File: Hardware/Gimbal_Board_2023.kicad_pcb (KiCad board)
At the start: 2 copper layers, 139 x 93.5 mm, 72 parts, among them J1 6P6C, J2 RJ45_LED_Shielded, Q1 Q_NMOS_GDS, Q2 Q_NMOS_GDS, Q3 Q_NMOS_GDS, Q4 Q_NMOS_GDS, Q5 Q_NMOS_GDS, Q6 Q_NMOS_GDS, Q7 Q_NMOS_GDS, SW1 SW_Push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

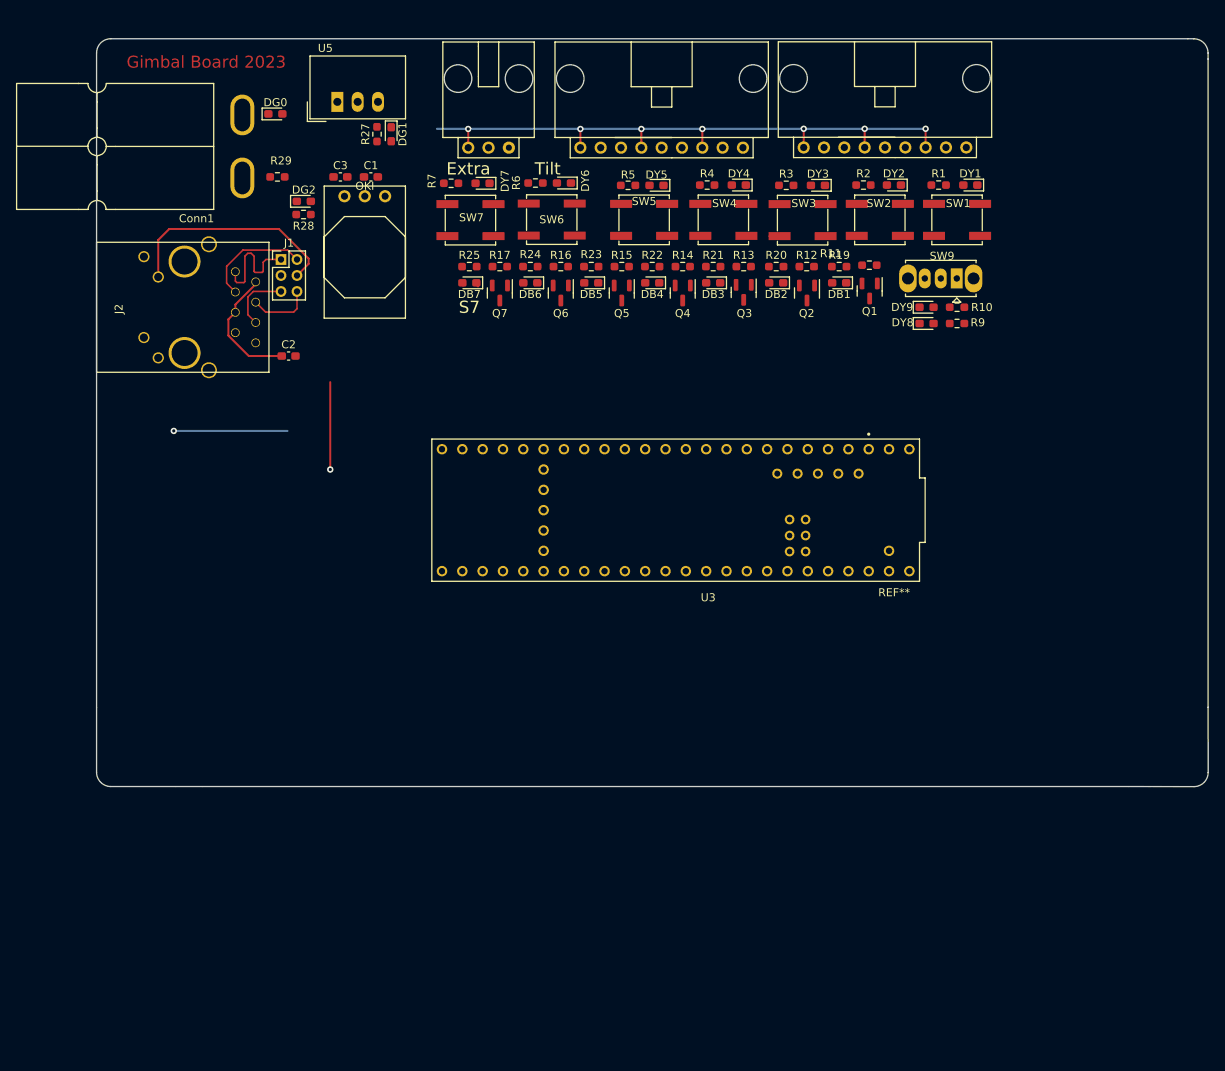
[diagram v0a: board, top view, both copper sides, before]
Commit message: Named some switches and added in volt line
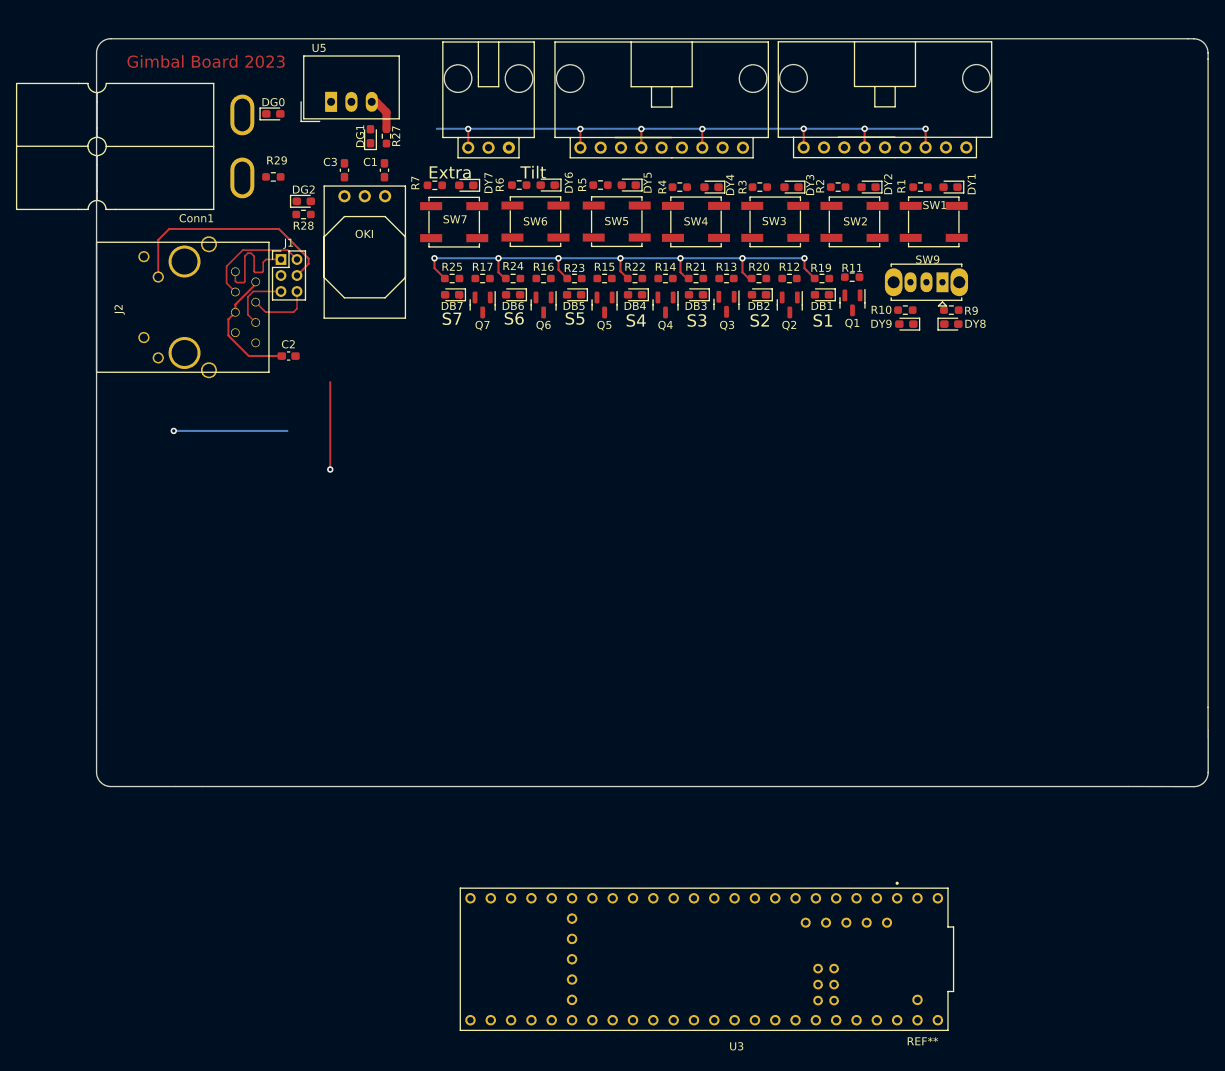
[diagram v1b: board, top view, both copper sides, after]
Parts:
- moved U3 56.2 mm to (191.0, 186.4)
- moved R10 6.47 mm to (165.4, 69.7)
- moved DY5 3.47 mm to (130.8, 54.1)
- moved R5 3.45 mm to (127.3, 54.1)
- moved DY4 3.43 mm to (141.1, 54.4)
- moved R4 3.43 mm to (137.2, 54.4)
- moved SW4 3.43 mm to (139.2, 58.7)
- moved SW3 3.43 mm to (149.1, 58.7)
- moved SW5 3.43 mm to (129.3, 58.7)
- moved DY3 3.31 mm to (151.1, 54.4)
- moved R3 3.31 mm to (147.2, 54.4)
- moved DY9 3.29 mm to (165.5, 71.5), turned to 180 degrees
- moved DY2 3.18 mm to (160.8, 54.4)
- moved R2 3.18 mm to (157.0, 54.4)
- moved SW2 3.18 mm to (159.0, 58.7)
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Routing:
- net +5V: track 77.6 -> 149.5 mm, vias 7 -> 14
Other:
- board text added: "S1"
- board text added: "S2"
- board text added: "S3"
- board text added: "S4"
- board text added: "S5"
- board text added: "S6"

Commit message: wiring
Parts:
- moved U3 67.6 mm to (187.7, 118.9)
- moved DY8 49.7 mm to (121.4, 71.3)
- moved DY9 49.7 mm to (115.8, 71.3)
- moved R10 49.7 mm to (115.7, 69.6)
- moved R9 49.7 mm to (121.4, 69.6)
- moved SW9 49.7 mm to (120.3, 66.1)
- moved Q3 30.5 mm to (173.5, 67.7)
- moved R13 30.5 mm to (173.5, 64.5)
- moved DB3 29.9 mm to (169.1, 66.5)
- moved R21 29.9 mm to (169.1, 64.5)
- moved Q6 28.0 mm to (148.1, 67.9)
- moved R16 28.0 mm to (148.1, 64.6)
- moved DB6 27.6 mm to (143.9, 66.6)
- moved R24 27.6 mm to (143.9, 64.6)
- moved Q2 14.0 mm to (164.9, 67.8)
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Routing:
- net +3.3V: track 0.00 -> 87.1 mm
- net Servo_7_SW: track 0.00 -> 33.0 mm, vias 0 -> 2
- net Servo_6_SW: track 0.00 -> 31.4 mm, vias 0 -> 2
- net +5V: track 149.5 -> 176.4 mm, vias 14 -> 2
- net +36V: track 1.23 -> 24.8 mm, vias 0 -> 2
- net Servo_7_PWM: track 0.00 -> 19.2 mm, vias 0 -> 1
- net Servo_1_PWM: track 0.00 -> 17.5 mm, vias 0 -> 1
- net Servo_2_PWM: track 0.00 -> 17.1 mm, vias 0 -> 1
- net Servo_3_PWM: track 0.00 -> 16.7 mm, vias 0 -> 1
- net Servo_6_PWM: track 0.00 -> 16.5 mm, vias 0 -> 1
- net Servo_4_PWM: track 0.00 -> 16.4 mm, vias 0 -> 1
- net Servo_5_PWM: track 0.00 -> 16.2 mm, vias 0 -> 1
- net Net-(DG0-Pad2): track 0.00 -> 9.11 mm
- net Net-(DG1-Pad2): track 0.00 -> 2.02 mm
- net Net-(DG2-Pad2): track 0.00 -> 1.65 mm

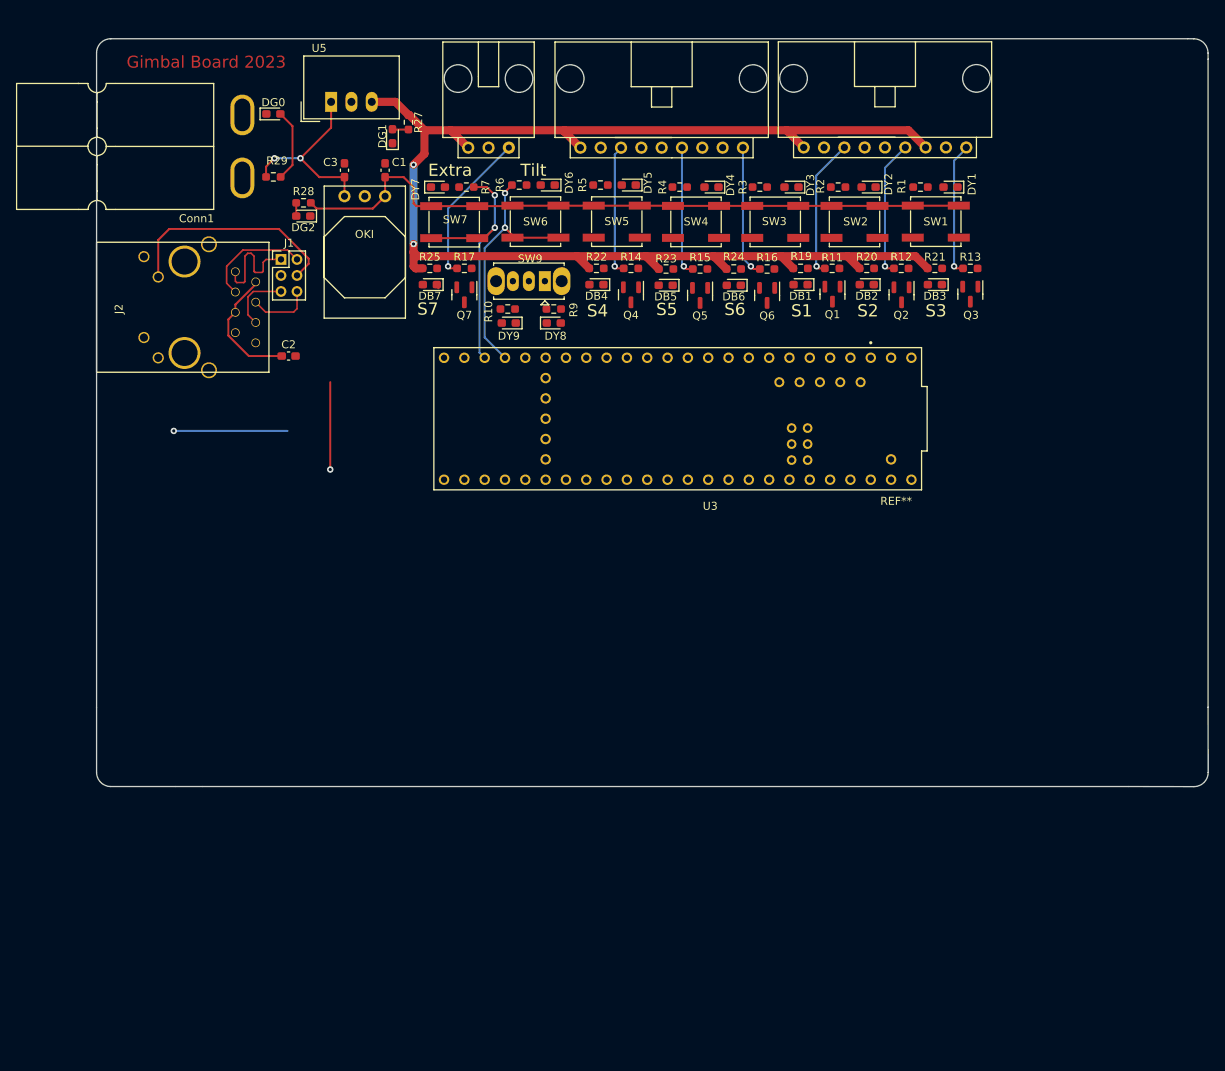
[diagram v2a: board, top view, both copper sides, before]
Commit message: Completed wiring and changed position of various pins
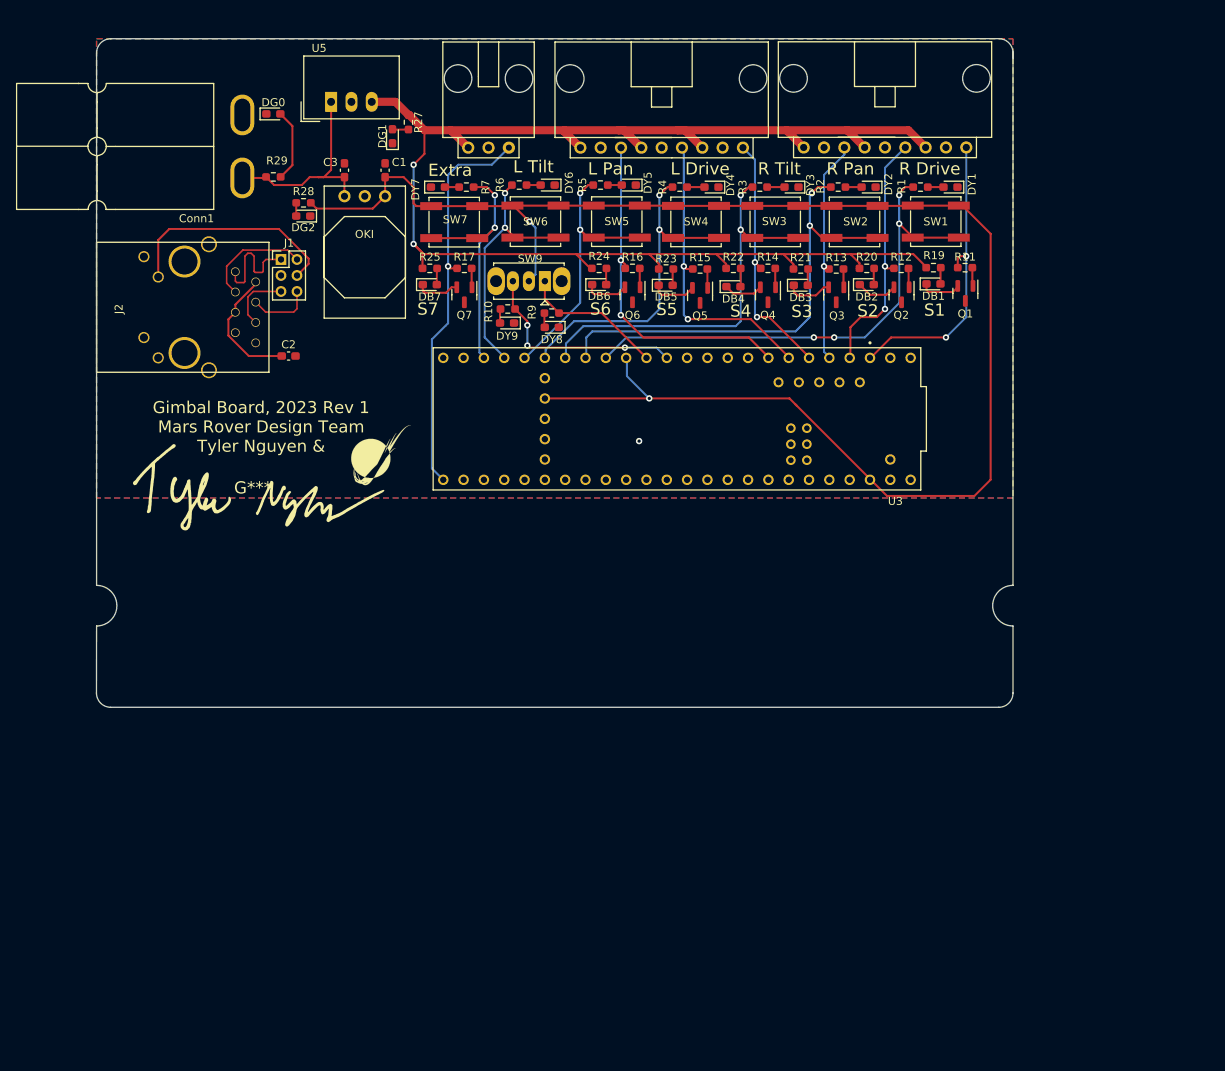
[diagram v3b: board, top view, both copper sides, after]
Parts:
- added G***: LOGO, MRDT_Silkscreens:0_MRDT_Logo_7.5mm, F.Cu at (99.8, 87.9)
- added G***: LOGO, Gimbal_Board_Library:z-sig-Tyler-Nguyen, F.Cu at (83.8, 91.9)
- U3: footprint MRDT_Shields:Teensy_4_1_Vertical -> MRDT_Shields:MODULE_DEV-16771
- moved U3 62.1 mm to (136.8, 83.3)
- moved DB4 17.1 mm to (143.9, 66.8), turned to 0 degrees
- moved R22 17.1 mm to (143.9, 64.5)
- moved Q4 17.1 mm to (148.2, 67.8)
- moved R14 17.1 mm to (148.2, 64.5)
- moved DB6 16.8 mm to (127.1, 66.5), turned to 0 degrees
- moved R24 16.8 mm to (127.1, 64.5)
- moved Q6 16.8 mm to (131.3, 67.8)
- moved R16 16.8 mm to (131.3, 64.5)
- moved DB3 16.8 mm to (152.3, 66.6), turned to 0 degrees
- moved Q3 16.8 mm to (156.7, 67.8)
- moved R13 16.8 mm to (156.7, 64.6)
- moved R21 16.8 mm to (152.3, 64.6)
- moved DB1 16.6 mm to (168.9, 66.5), turned to 0 degrees
- moved R19 16.6 mm to (168.9, 64.4)
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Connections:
- Conn6 pad 3: Servo_1_PWM -> Servo_3_PWM
- Conn6 pad 9: Servo_3_PWM -> Servo_1_PWM
- Conn7 pad 3: Servo_4_PWM -> Servo_6_PWM
- Conn7 pad 9: Servo_6_PWM -> Servo_4_PWM
- U3 pad 33: unconnected-(U3-Pad33) -> Servo_7_PWM
- U3 pad 7: Servo_7_PWM -> unconnected-(U3-Pad7)
- U3 pad 8: (no net) -> unconnected-(U3-Pad8)
- U3 pad GND1: (no net) -> GND
- U3 pad GND2: (no net) -> GND
- U3 pad GND3: (no net) -> GND
- U3 pad GND4: (no net) -> GND
- U3 pad GND5: (no net) -> GND
- U3 pad USB_GND1: (no net) -> GND
- U3 pad USB_GND2: (no net) -> GND
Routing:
- net +3.3V: track 87.1 -> 202.2 mm, vias 0 -> 2
- net Servo_1_SW: track 0.00 -> 64.2 mm, vias 0 -> 4
- net Servo_2_SW: track 0.00 -> 58.9 mm, vias 0 -> 2
- net Servo_3_SW: track 1.46 -> 51.5 mm, vias 0 -> 2
- net Servo_4_SW: track 0.00 -> 41.5 mm, vias 0 -> 2
- net Servo_5_SW: track 0.00 -> 33.3 mm, vias 0 -> 2
- net Servo_7_PWM: track 19.2 -> 49.8 mm
- net Servo_Manual_Control_Right: track 0.00 -> 26.9 mm, vias 0 -> 3
- net Servo_6_PWM: track 16.5 -> 43.2 mm, vias 1 -> 2
- net (no net): track 25.5 -> 0.32 mm, vias 2 -> 0
- net Servo_5_PWM: track 16.2 -> 37.7 mm, vias 1 -> 2
- net Servo_1_PWM: track 17.5 -> 37.6 mm, vias 1 -> 2
- net Servo_Manual_Control_Left: track 0.00 -> 18.0 mm
- net Servo_4_PWM: track 16.4 -> 31.7 mm, vias 1 -> 2
- net Servo_2_PWM: track 17.1 -> 31.5 mm, vias 1 -> 2
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- added copper zone on B.Cu, net GND
- added copper zone on F.Cu, net GND
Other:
- board size 139 x 93.5 mm -> 114.6 x 83.6 mm
- board text added: "Gimbal Board, 2023 Rev 1 Mars Rover Design Team Tyler Nguyen &"
- board text added: "L Drive"
- board text added: "L Pan"
- board text added: "L Tilt"
- board text added: "R Drive"
- board text added: "R Pan"
- board text added: "R Tilt"
- board text removed: "Gimbal Board 2023"
- board text removed: "Tilt"

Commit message: Rewired trace and labeled diodes
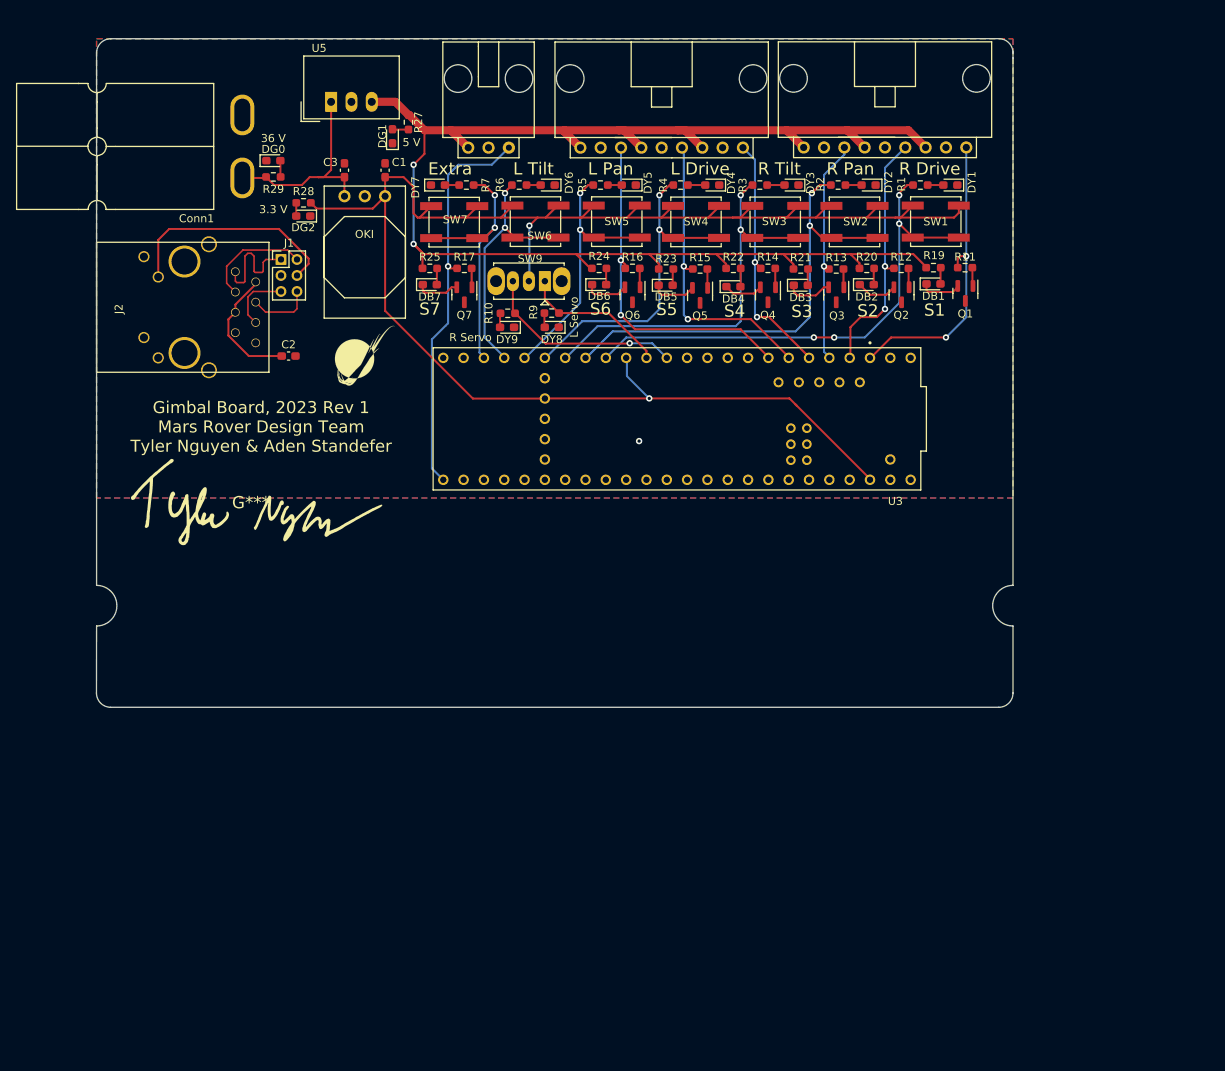
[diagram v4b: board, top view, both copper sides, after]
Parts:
- moved G*** 12.6 mm to (97.8, 75.4)
- moved DG0 5.84 mm to (86.4, 51.1)
- moved G*** 1.86 mm to (83.6, 93.8)
- moved DY9 0.54 mm to (115.6, 71.9)
- moved R10 0.54 mm to (115.7, 70.1)
- moved DY4 0.27 mm to (141.2, 54.1)
- moved R4 0.27 mm to (137.3, 54.1)
- moved DY1 0.25 mm to (171.0, 54.1)
- moved R1 0.25 mm to (167.2, 54.1)
- moved DY2 0.25 mm to (160.8, 54.1)
- moved DY3 0.25 mm to (151.1, 54.1)
- moved DY7 0.25 mm to (106.9, 54.1)
- moved R2 0.25 mm to (157.0, 54.1)
- moved R3 0.25 mm to (147.2, 54.1)
- moved R7 0.25 mm to (110.5, 54.1)
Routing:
- net +3.3V: track 202.2 -> 219.6 mm
- net Net-(DG0-Pad2): track 9.11 -> 2.05 mm
- net Servo_Manual_Control_Right: track 26.9 -> 25.4 mm, vias 3 -> 1
- net Servo_2_SW: track 58.9 -> 57.5 mm
- net Servo_3_SW: track 51.5 -> 50.6 mm
- net Servo_Manual_Control_Left: track 18.0 -> 18.5 mm
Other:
- board text added: "3.3 V"
- board text added: "36 V"
- board text added: "5 V"
- board text added: "Gimbal Board, 2023 Rev 1 Mars Rover Design Team Tyler Nguyen & Aden Standefer"
- board text added: "L Servo"
- board text added: "R Servo"
- board text removed: "Gimbal Board, 2023 Rev 1 Mars Rover Design Team Tyler Nguyen &"

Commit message: rewired 3.3 v line to the switches and redrew edgecuts
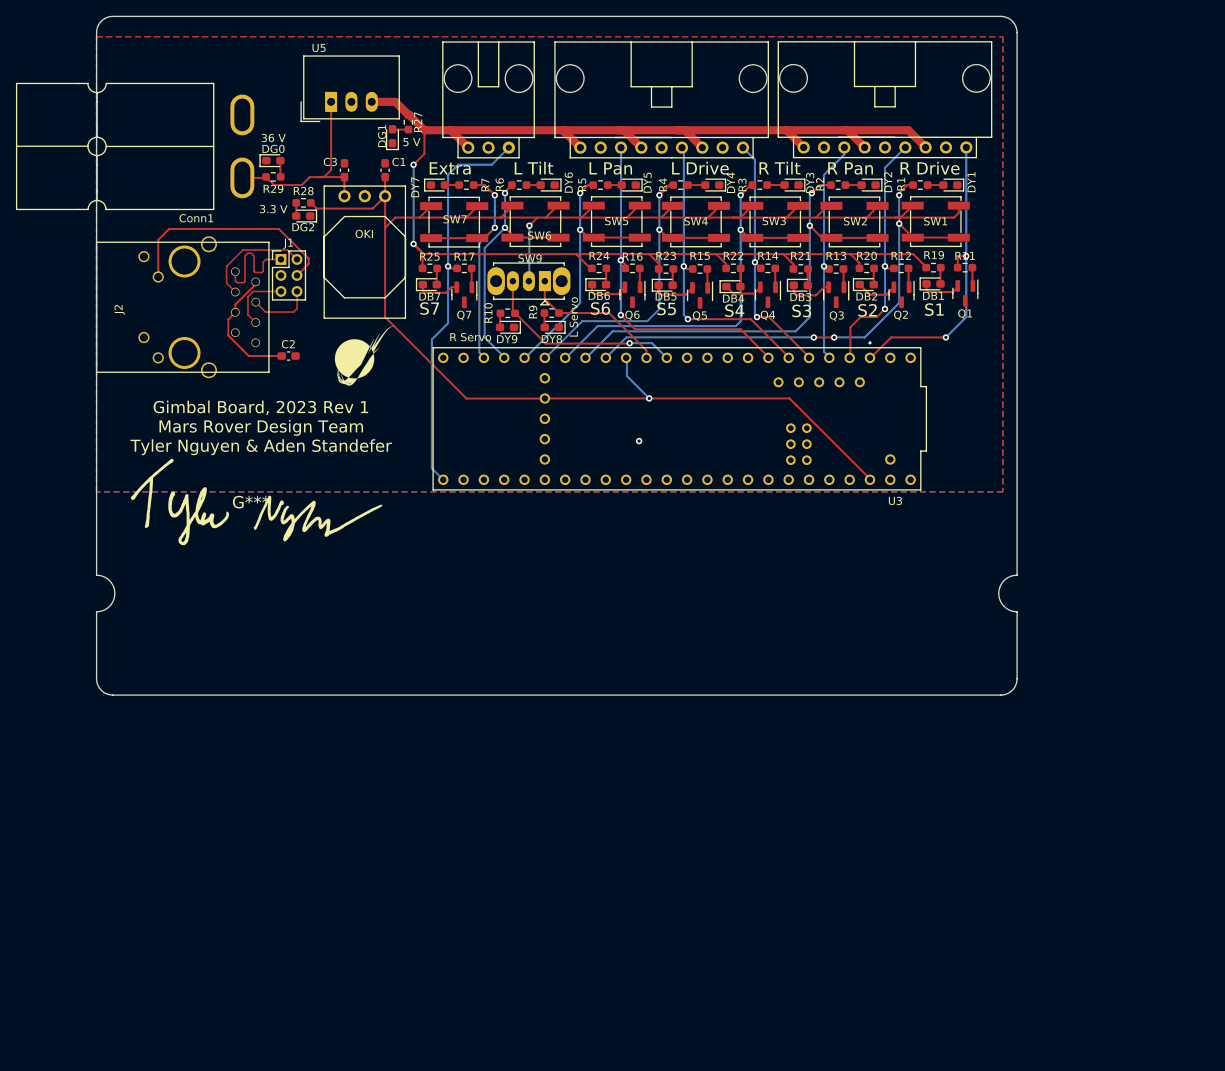
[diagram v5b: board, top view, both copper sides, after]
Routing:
- net +3.3V: track 219.6 -> 218.3 mm
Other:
- board size 114.6 x 83.6 mm -> 115.1 x 84.8 mm
